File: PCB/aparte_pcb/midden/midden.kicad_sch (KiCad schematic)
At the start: 29 parts

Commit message: p
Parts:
- teensy1: footprint teensy.pretty-master:Teensy41 -> Library:Teensy41
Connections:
- net GND: no longer D5.2 (A)
- net groundd: now reaches 3V3_conv1.4 (GND), 3V3_conv1.5 (GND), 5V_conv1.4 (GND), 5V_conv1.5 (GND), D10.1 (K), D14.1 (K), D15.1 (K), D7.2 (A)
- net 12V: no longer names the net of D4.1 (K)
- net S: no longer names the net of teensy1.39 (17_A3_TX4_SDA1)
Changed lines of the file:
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@@
+		)
+	)
+	(global_label "groundd"
+		(shape input)
+		(at 90.17 113.03 270)
+		(fields_autoplaced yes)
+		(effects
+			(font
+				(size 1.27 1.27)
+			)
+			(justify right)
+		)
+		(property "Intersheetrefs" "${INTERSHEET_REFS}"
+			(at 90.17 123.6954 90)
+			(effects
+				(font
+					(size 1.27 1.27)
+				)
+				(justify right)
+				(hide yes)
+			)
 		)
 	)
@@
 		)
 	)
-	(global_label "GND"
+	(global_label "pr2"
 		(shape input)
-		(at 66.04 154.94 0)
+		(at 303.53 107.95 180)
 		(fields_autoplaced yes)
 		(effects
@@
 				(size 1.27 1.27)
 			)
-			(justify left)
+			(justify right)
 		)
 		(property "Intersheetrefs" "${INTERSHEET_REFS}"
-			(at 72.8957 154.94 0)
-			(effects
-				(font
-					(size 1.27 1.27)
-				)
-				(justify left)
-				(hide yes)
-			)
-		)
-	)
-	(global_label "pr2"
+			(at 297.4001 107.95 0)
+			(effects
+				(font
+					(size 1.27 1.27)
+				)
+				(justify right)
+				(hide yes)
+			)
+		)
+	)
+	(global_label "5V"
 		(shape input)
-		(at 303.53 107.95 180)
+		(at 303.53 135.89 180)
 		(fields_autoplaced yes)
 		(effects
@@
 		)
 		(property "Intersheetrefs" "${INTERSHEET_REFS}"
-			(at 297.4001 107.95 0)
+			(at 298.2467 135.89 0)
 			(effects
 				(font
@@
 		)
 	)
-	(global_label "5V"
+	(global_label "pr6"
 		(shape input)
-		(at 303.53 135.89 180)
+		(at 303.53 118.11 180)
 		(fields_autoplaced yes)
 		(effects
@@
 		)
 		(property "Intersheetrefs" "${INTERSHEET_REFS}"
-			(at 298.2467 135.89 0)
+			(at 297.4001 118.11 0)
 			(effects
 				(font
@@
 		)
 	)
-	(global_label "pr6"
+	(global_label "tx3"
 		(shape input)
-		(at 303.53 118.11 180)
+		(at 184.15 21.59 270)
 		(fields_autoplaced yes)
 		(effects
@@
 		)
 		(property "Intersheetrefs" "${INTERSHEET_REFS}"
-			(at 297.4001 118.11 0)
+			(at 184.15 27.5385 90)
 			(effects
 				(font
@@
 		)
 	)
-	(global_label "tx3"
+	(global_label "5v"
 		(shape input)
-		(at 184.15 21.59 270)
+		(at 201.93 21.59 270)
 		(fields_autoplaced yes)
 		(effects
@@
 		)
 		(property "Intersheetrefs" "${INTERSHEET_REFS}"
-			(at 184.15 27.5385 90)
+			(at 201.93 26.7523 90)
 			(effects
 				(font
@@
 		)
 	)
-	(global_label "5v"
+	(global_label "3v3"
 		(shape input)
-		(at 201.93 21.59 270)
+		(at 199.39 21.59 270)
 		(fields_autoplaced yes)
 		(effects
@@
 		)
 		(property "Intersheetrefs" "${INTERSHEET_REFS}"
-			(at 201.93 26.7523 90)
+			(at 199.39 27.9618 90)
 			(effects
 				(font
@@
 		)
 	)
-	(global_label "3v3"
+	(global_label "rx2"
 		(shape input)
-		(at 199.39 21.59 270)
+		(at 186.69 21.59 270)
 		(fields_autoplaced yes)
 		(effects
@@
 		)
 		(property "Intersheetrefs" "${INTERSHEET_REFS}"
-			(at 199.39 27.9618 90)
+			(at 186.69 27.599 90)
 			(effects
 				(font
@@
 				)
 				(justify right)
-				(hide yes)
-			)
-		)
-	)
-	(global_label "rx2"
-		(shape input)
-		(at 186.69 21.59 270)
-		(fields_autoplaced yes)
-		(effects
-			(font
-				(size 1.27 1.27)
-			)
-			(justify right)
-		)
-		(property "Intersheetrefs" "${INTERSHEET_REFS}"
-			(at 186.69 27.599 90)
-			(effects
-				(font
-					(size 1.27 1.27)
-				)
-				(justify right)
-				(hide yes)
-			)
-		)
-	)
-	(global_label "S"
-		(shape input)
-		(at 73.66 154.94 0)
-		(fields_autoplaced yes)
-		(effects
-			(font
-				(size 1.27 1.27)
-			)
-			(justify left)
-		)
-		(property "Intersheetrefs" "${INTERSHEET_REFS}"
-			(at 77.8547 154.94 0)
-			(effects
-				(font
-					(size 1.27 1.27)
-				)
-				(justify left)
-				(hide yes)
-			)
-		)
-	)
-	(global_label "12V"
-		(shape input)
-		(at 58.42 154.94 0)
-		(fields_autoplaced yes)
-		(effects
-			(font
-				(size 1.27 1.27)
-			)
-			(justify left)
-		)
-		(property "Intersheetrefs" "${INTERSHEET_REFS}"
-			(at 64.9128 154.94 0)
-			(effects
-				(font
-					(size 1.27 1.27)
-				)
-				(justify left)
 				(hide yes)
 			)
@@
 			)
 		)
-		(property "Footprint" "teensy.pretty-master:Teensy41"
+		(property "Footprint" "Library:Teensy41"
 			(at 199.39 111.76 0)
 			(effects

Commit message: pxb
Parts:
- added D17, D18: D, Diode_SMD:D_MELF-RM10_Universal_Handsoldering, symbol Library:D
- added J1, J4: Conn_01x10_Socket, Connector_JST:JST_EH_S10B-EH_1x10_P2.50mm_Horizontal, symbol Connector:Conn_01x10_Socket
- added J5: Conn_01x04_Socket, Connector_JST:JST_EH_S4B-EH_1x04_P2.50mm_Horizontal, symbol Connector:Conn_01x04_Socket
- added SW1: SW_Reed_SPDT, Connector_PinHeader_1.27mm:PinHeader_1x03_P1.27mm_Vertical, symbol Switch:SW_Reed_SPDT
- added SW2: SW_DIP_x01, dpdsd:R1966ABLKBLKEF, symbol Switch:SW_DIP_x01
- added U1: ~, Library:miniIMU, symbol New_Library:miniIMU
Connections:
- net 3v3: now also J1.9 (Pin_9)
- net 5V: now also J5.3 (Pin_3)
- net 5v: now also J1.10 (Pin_10)
- net BLAUW: now also J5.1 (Pin_1)
- net GND: now also J5.2 (Pin_2)
- net GROEN: now also J4.10 (Pin_10)
- net ROOD: now also J4.9 (Pin_9)
- net gnd: now also J1.8 (Pin_8)
- net groundd: now also D18.1 (K), SW1.1
- net pr1: now also J4.1 (Pin_1)
- net pr2: now also J4.2 (Pin_2)
- net pr3: now also J4.3 (Pin_3)
- net pr4: now also J4.4 (Pin_4)
- net pr5: now also J4.5 (Pin_5)
- net pr6: now also J4.6 (Pin_6)
- net pr7: now also J4.7 (Pin_7)
- net pr8: now also J4.8 (Pin_8)
- net rx1: now also J1.6 (Pin_6)
- net rx2: now also J1.4 (Pin_4)
- net rx3: now also J1.2 (Pin_2)
- net soft_power_sw: now also J1.1 (Pin_1)
- net tx1: now also J1.7 (Pin_7)
- net tx2: now also J1.5 (Pin_5)
- net tx3: now also J1.3 (Pin_3)
- net at D12.2 (A), D13.2 (A), D16.2 (A)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: now also D17.2 (A)
- net at D1.1 (K): now also SW2.1; no longer F1.2
- net at teensy1.40 (18_A4_SDA): now also U1.2 (sda)
- net at teensy1.41 (19_A5_SCL): now also U1.1 (scl)
- net at teensy1.44 (22_A8_CTX1): now also SW1.2
- new net: F1.2, SW2.2
- new net: D18.2 (A), U1.3 (gnd)
- new net: D17.1 (K), U1.4 (vin)
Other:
- moved on the sheet: F1

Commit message: kicker
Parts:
- added C1: C, Capacitor_THT:CP_Radial_D8.0mm_P3.50mm, symbol Device:C
- added K1: G5Q-1A, Relay_THT:Relay_SPST_Omron-G5Q-1A, symbol Relay:G5Q-1A
- solenoid1: footprint (none) -> TerminalBlock_Altech:Altech_AK100_1x02_P5.00mm
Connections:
- net at D4.1 (K): now also C1.1
- net at D5.2 (A): now also solenoid1.2 (-)
- net at solenoid1.1 (+): now also K1.2
- net at teensy1.39 (17_A3_TX4_SDA1): now also K1.5
- net at teensy1.42 (20_A6_TX5_LRCLK1): now also K1.1
- new net: C1.2, K1.3
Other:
- moved on the sheet: solenoid1

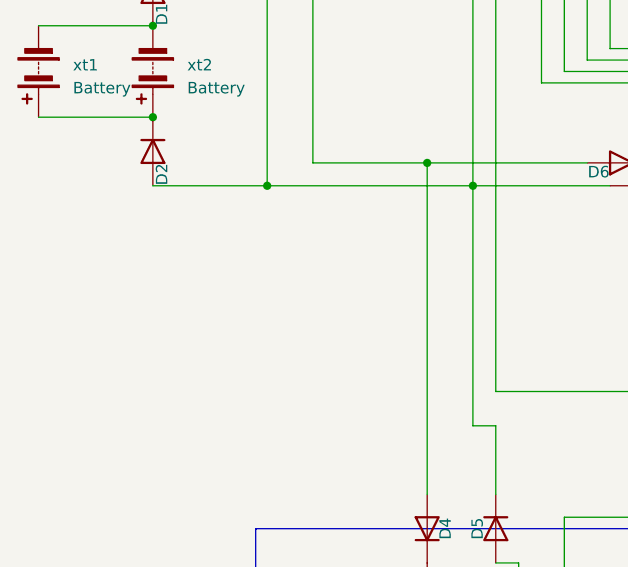
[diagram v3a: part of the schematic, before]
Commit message: schroef geaard
moet nog onderste schroef
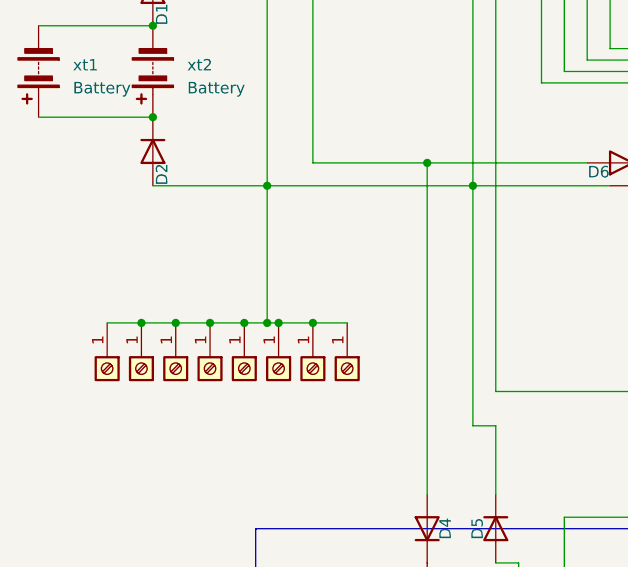
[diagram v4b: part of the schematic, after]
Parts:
- added J10, J11, J2, J3, J6, J7, J8, J9: Screw_Terminal_01x01, MountingHole:MountingHole_4.3mm_M4_ISO7380_Pad, symbol Connector:Screw_Terminal_01x01
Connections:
- net at D2.2 (A), D3.2 (A), D5.1 (K)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: now also J10.1 (Pin_1), J11.1 (Pin_1), J2.1 (Pin_1), J3.1 (Pin_1), J6.1 (Pin_1), J7.1 (Pin_1), J8.1 (Pin_1), J9.1 (Pin_1)

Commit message: dgsrf
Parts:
- added SW5: SW_Reed_SPDT, Library:Mini Snap-Action Switch with 13.5mm Lever 3-Pin, SPDT, 1A, symbol Switch:SW_Reed_SPDT
- 3V3_conv1, 5V_conv1: footprint Library:pololu-U1V10F5 -> Library:pololu-d30v30fx
- SW1: footprint Connector_PinHeader_1.27mm:PinHeader_1x03_P1.27mm_Vertical -> Library:Mini Snap-Action Switch with 13.5mm Lever 3-Pin, SPDT, 1A
- SW2: footprint dpdsd:R1966ABLKBLKEF -> Library:Rocker Switch 3-Pin, SPDT, 10A
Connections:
- net groundd: now also SW5.1
- net at teensy1.43 (21_A7_RX5_BCLK1): now also SW5.2
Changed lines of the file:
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@@
 	)
 	(junction
+		(at 259.08 86.36)
+		(diameter 0)
+		(color 0 0 0 0)
+	)
+	(junction
 		(at 63.5 80.01)
 		(diameter 0)
@@
 	(wire
 		(pts
+			(xy 259.08 86.36) (xy 259.08 133.35)
+		)
+		(stroke
+			(width 0)
+			(type default)
+		)
+	)
+	(wire
+		(pts
 			(xy 86.36 31.75) (xy 86.36 44.45)
 		)
@@
 	(wire
 		(pts
-			(xy 243.84 77.47) (xy 237.49 77.47)
-		)
-		(stroke
-			(width 0)
-			(type default)
-		)
-	)
-	(wire
-		(pts
 			(xy 63.5 80.01) (xy 63.5 113.03)
 		)
@@
 	(wire
 		(pts
+			(xy 237.49 77.47) (xy 243.84 77.47)
+		)
+		(stroke
+			(width 0)
+			(type default)
+		)
+	)
+	(wire
+		(pts
 			(xy 146.05 33.02) (xy 146.05 46.99)
 		)
@@
 	(wire
 		(pts
+			(xy 243.84 80.01) (xy 243.84 88.9)
+		)
+		(stroke
+			(width 0)
+			(type default)
+		)
+	)
+	(wire
+		(pts
 			(xy 153.67 125.73) (xy 181.61 125.73)
 		)
@@
 	(wire
 		(pts
-			(xy 259.08 74.93) (xy 259.08 133.35)
+			(xy 259.08 74.93) (xy 259.08 86.36)
 		)
 		(stroke
@@
 	(wire
 		(pts
+			(xy 256.54 86.36) (xy 259.08 86.36)
+		)
+		(stroke
+			(width 0)
+			(type default)
+		)
+	)
+	(wire
+		(pts
 			(xy 59.69 46.99) (xy 59.69 29.21)
 		)
@@
 	(wire
 		(pts
+			(xy 237.49 80.01) (xy 243.84 80.01)
+		)
+		(stroke
+			(width 0)
+			(type default)
+		)
+	)
+	(wire
+		(pts
 			(xy 278.13 113.03) (xy 307.34 113.03)
 		)
@@
 			)
 		)
-		(property "Footprint" "Library:pololu-U1V10F5"
+		(property "Footprint" "Library:pololu-d30v30fx"
 			(at 101.6 105.41 0)
 			(effects
@@
 			)
 		)
-		(property "Footprint" "Library:pololu-U1V10F5"
+		(property "Footprint" "Library:pololu-d30v30fx"
 			(at 102.87 111.76 0)
 			(effects
@@
 			)
 		)
-		(property "Footprint" "dpdsd:R1966ABLKBLKEF"
+		(property "Footprint" "Library:Rocker Switch 3-Pin, SPDT, 10A"
 			(at 27.94 80.01 0)
 			(effects
@@
 			)
 		)
-		(property "Footprint" "Connector_PinHeader_1.27mm:PinHeader_1x03_P1.27mm_Vertical"
+		(property "Footprint" "Library:Mini Snap-Action Switch with 13.5mm Lever 3-Pin, SPDT, 1A"
 			(at 248.92 77.47 0)
 			(effects
@@
 					(unit 1)
 				)
+			)
+		)
+	)
+	(symbol
+		(lib_id "Switch:SW_Reed_SPDT")
+		(at 248.92 88.9 0)
+		(unit 1)
+		(exclude_from_sim no)
+		(in_bom yes)
+		(on_board yes)
+		(dnp no)
+		(fields_autoplaced yes)
+		(property "Reference" "SW5"
+			(at 249.6215 81.28 0)
+			(effects
+				(font
+					(size 1.27 1.27)
+				)
+				(hide yes)
+			)
+		)
+		(property "Value" "SW_Reed_SPDT"
+			(at 249.6215 83.82 0)
+			(effects
+				(font
+					(size 1.27 1.27)
+				)
+				(hide yes)
+			)
+		)
+		(property "Footprint" "Library:Mini Snap-Action Switch with 13.5mm Lever 3-Pin, SPDT, 1A"
+			(at 248.92 88.9 0)
+			(effects
+				(font
+					(size 1.27 1.27)
+				)
+				(hide yes)
+			)
+		)
+		(property "Datasheet" "~"
+			(at 248.92 88.9 0)
+			(effects
+				(font
+					(size 1.27 1.27)
+				)
+				(hide yes)
+			)
+		)
+		(property "Description" "SPDT reed switch"
+			(at 248.92 88.9 0)
+			(effects
+				(font
+					(size 1.27 1.27)
+				)
+				(hide yes)
+			)
+		)
+		(pin "3"
+		)
+		(pin "1"
+		)
+		(pin "2"
+		)
+		(instances
+			(project "midden"
+				(path "/e189b955-7e7c-46c1-a031-b30377455d70"
+					(reference "SW5")
+					(unit 1)
+				)
